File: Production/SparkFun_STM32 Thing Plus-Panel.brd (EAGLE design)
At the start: 145 x 106.7 mm, 998 parts, among them J10 QWIIC_RA, J13 CORTEX_DEBUG, J14 MICRO-SD, J17 QWIIC_RA, J20 CORTEX_DEBUG, J21 MICRO-SD, J24 QWIIC_RA, J27 CORTEX_DEBUG, J28 MICRO-SD, J3 QWIIC_RA, J31 QWIIC_RA, J34 CORTEX_DEBUG, J35 MICRO-SD, J38 QWIIC_RA, J41 CORTEX_DEBUG, J42 MICRO-SD, J45 QWIIC_RA, J48 CORTEX_DEBUG, J49 MICRO-SD, J52 QWIIC_RA, J55 CORTEX_DEBUG, J56 MICRO-SD, J6 CORTEX_DEBUG, J7 MICRO-SD, U1 MCP73831, U10 MCP73831, U11 3.3V, U12 W25QXX128MBIT-6X5, U13 STM32F405RGT6, U14 MCP73831, U15 3.3V, U16 W25QXX128MBIT-6X5, U17 STM32F405RGT6, U18 MCP73831, U19 3.3V, U2 3.3V, U20 W25QXX128MBIT-6X5, U21 STM32F405RGT6, U22 MCP73831, U23 3.3V, U24 W25QXX128MBIT-6X5, U25 STM32F405RGT6, U26 MCP73831, U27 3.3V, U28 W25QXX128MBIT-6X5, U29 STM32F405RGT6, U3 W25QXX128MBIT-6X5, U30 MCP73831, U31 3.3V, U32 W25QXX128MBIT-6X5, U4 STM32F405RGT6, U5 STM32F405RGT6, U6 MCP73831, U7 3.3V, U8 W25QXX128MBIT-6X5, U9 STM32F405RGT6, Y1 32.768kHz, Y10 12MHz, Y11 32.768kHz, Y12 12MHz, Y13 32.768kHz, Y14 12MHz, Y15 32.768kHz, Y16 12MHz, Y2 12MHz, Y3 32.768kHz, Y4 12MHz, Y5 32.768kHz, Y6 12MHz, Y7 32.768kHz, Y8 12MHz, Y9 32.768kHz

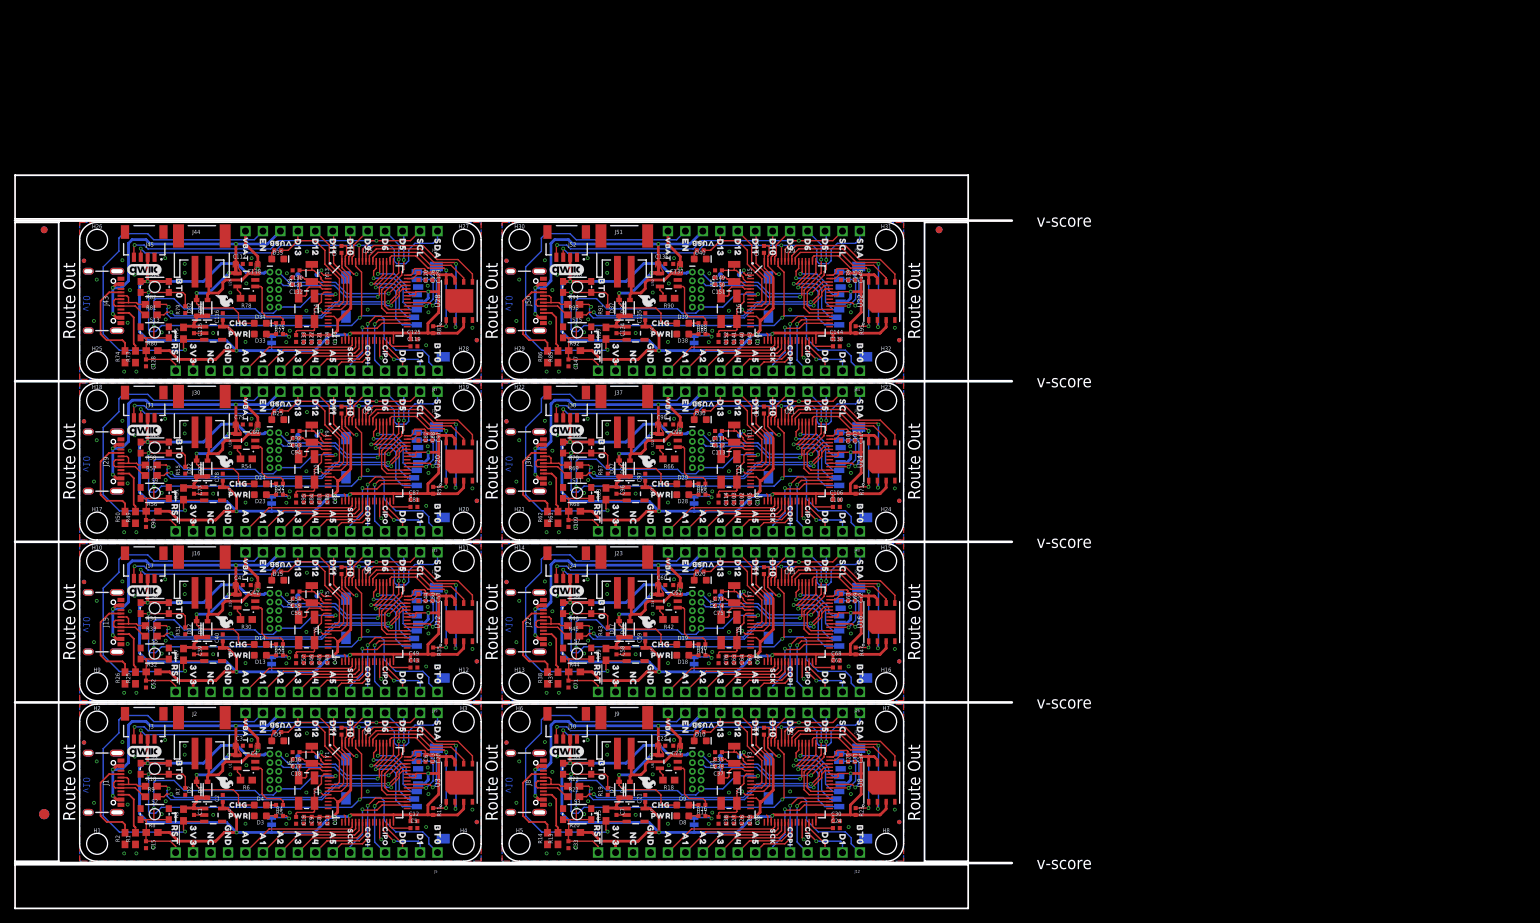
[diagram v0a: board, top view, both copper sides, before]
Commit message: Updated Panel
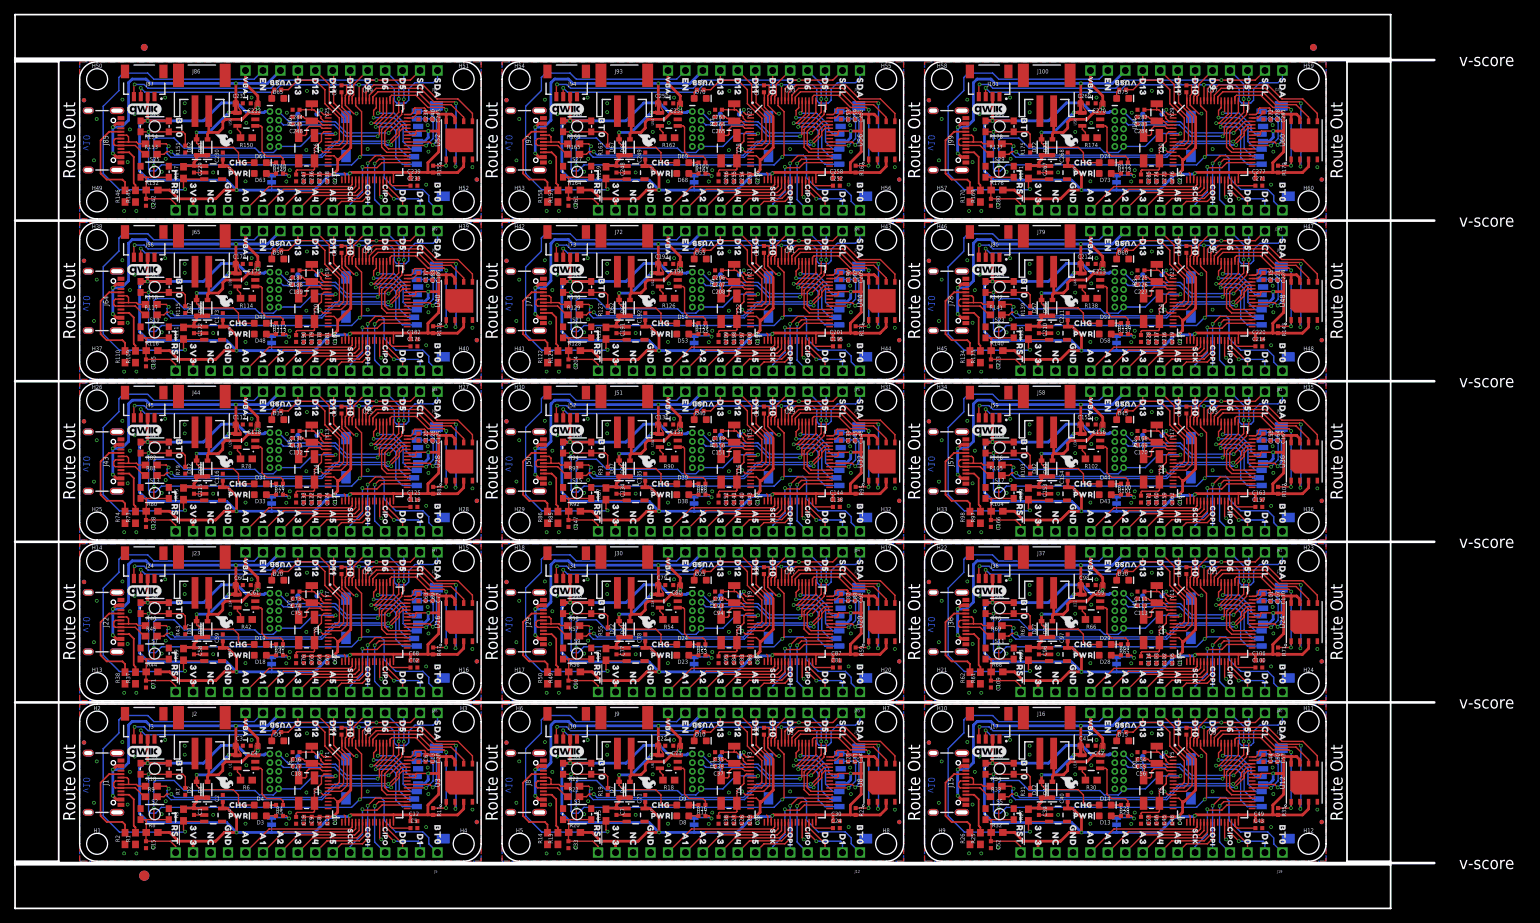
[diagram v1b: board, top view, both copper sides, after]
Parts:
- added C153, C154, C160, C172, C173, C179, C191, C192, C198, C210, C211, C217, C229, C230, C236, C248, C249, C255, C267, C268, C274: 1.0uF, SparkFun-Capacitors:0402-TIGHT
- added C155, C156, C161, C174, C175, C180, C193, C194, C199, C212, C213, C218, C231, C232, C237, C250, C251, C256, C269, C270, C275: 4.7uF, SparkFun-Capacitors:0402-TIGHT
- added C157, C158, C176, C177, C195, C196, C214, C215, C233, C234, C252, C253, C271, C272: 2.2uF, SparkFun-Capacitors:0402-TIGHT
- added C159, C162, C163, C164, C165, C166, C167, C178, C181, C182, C183, C184, C185, C186, C197, C200, C201, C202, C203, C204, C205, C216, C219, C220, C221, C222, C223, C224, C235, C238, C239, C240, C241, C242, C243, C254, C257, C258, C259, C260, C261, C262, C273, C276, C277, C278, C279, C280, C281: 0.1uF, SparkFun-Capacitors:0402-TIGHT
- added C168, C169, C187, C188, C206, C207, C225, C226, C244, C245, C263, C264, C282, C283: 15pF, SparkFun-Capacitors:0402-TIGHT
- added C170, C171, C189, C190, C208, C209, C227, C228, C246, C247, C265, C266, C284, C285: 22pF, SparkFun-Capacitors:0402-TIGHT
- added D41, D42, D46, D47, D51, D52, D56, D57, D61, D62, D66, D67, D71, D72: 3A/10V/280mV, SparkFun-DiscreteSemi:SOD-323
- added D43, D48, D53, D58, D63, D68, D73: RED, SparkFun-LED:LED-0603
- added D44, D49, D54, D59, D64, D69, D74: Yellow, SparkFun-LED:LED-0603
- added D45, D50, D55, D60, D65, D70, D75: BLUE, SparkFun-LED:LED-0603
- added FD33, FD34, FD35, FD36, FD37, FD38, FD39, FD40, FD41, FD42, FD43, FD44, FD45, FD46, FD47, FD48, FD49, FD50, FD51, FD52, FD53, FD54, FD55, FD56, FD57, FD58, FD59, FD60: FIDUCIALUFIDUCIAL, SparkFun-Aesthetics:FIDUCIAL-MICRO
- added H33, H34, H35, H36, H37, H38, H39, H40, H41, H42, H43, H44, H45, H46, H47, H48, H49, H50, H51, H52, H53, H54, H55, H56, H57, H58, H59, H60: STAND-OFFTIGHT, SparkFun-Hardware:STAND-OFF-TIGHT
- added J100, J58, J65, J72, J79, J86, J93: (no value), SparkFun-Connectors:JST-2-SMD
- added J101, J59, J66, J73, J80, J87, J94: QWIIC_RA, SparkFun-Connectors:JST04_1MM_RA
- added J102, J60, J67, J74, J81, J88, J95: (no value), SparkFun-Connectors:1X12_SM_SQ_NOSILK
- added J103, J61, J68, J75, J82, J89, J96: (no value), SparkFun-Connectors:1X16_SM_SQ_NOSILK
- added J104, J62, J69, J76, J83, J90, J97: CORTEX_DEBUG, SparkFun-Connectors:2X5-PTH-1.27MM-NO_SILK
- added J105, J63, J70, J77, J84, J91, J98: MICRO-SD, SparkFun-Connectors:MICRO-SD-SOCKET
- added J57, J64, J71, J78, J85, J92, J99: (no value), SparkFun-Connectors:USB-C-16P-2LAYER-PADS
- added LOGO25, LOGO28, LOGO31, LOGO34, LOGO37, LOGO40, LOGO43: QWIIC_LOGO_5MM, SparkFun-Aesthetics:QWIIC_5MM
- added LOGO26, LOGO29, LOGO32, LOGO35, LOGO38, LOGO41, LOGO44: SFE_LOGO_NAME_FLAME.1_INCH, SparkFun-Aesthetics:SFE_LOGO_NAME_FLAME_.1
- added LOGO27, LOGO30, LOGO33, LOGO36, LOGO39, LOGO42, LOGO45: OSHW-LOGOS, SparkFun-Aesthetics:OSHW-LOGO-S
- added PWR10, PWR11, PWR12, PWR13, PWR14, PWR8, PWR9: (no value), SparkFun-Jumpers:SMT-JUMPER_2_NC_TRACE_NO-SILK
- added R100, R101, R108, R112, R113, R120, R124, R125, R132, R136, R137, R144, R148, R149, R156, R160, R161, R168, R172, R173, R180: 1k, SparkFun-Resistors:0402-TIGHT
- added R102, R114, R126, R138, R150, R162, R174: 2.0k, SparkFun-Resistors:0603
- added R103, R107, R115, R119, R127, R131, R139, R143, R151, R155, R163, R167, R175, R179: 100k, SparkFun-Resistors:0402-TIGHT
- added R104, R116, R128, R140, R152, R164, R176: 4.7k, SparkFun-Resistors:0603
- added R105, R106, R117, R118, R129, R130, R141, R142, R153, R154, R165, R166, R177, R178: 22, SparkFun-Resistors:0603
- added R109, R110, R121, R122, R133, R134, R145, R146, R157, R158, R169, R170, R97, R98: 5.1k, SparkFun-Resistors:0603
- added R111, R123, R135, R147, R159, R171, R99: 10k, SparkFun-Resistors:0603
- added S17, S18, S19, S20, S21, S22, S23, S24, S25, S26, S27, S28, S29, S30: (no value), SparkFun-Switches:TACTILE_SWITCH_SMD_4.6X2.8MM
- added TP17, TP18, TP19, TP20, TP21, TP22, TP23, TP24, TP25, TP26, TP27, TP28, TP29, TP30, VB10, VB11, VB12, VB13, VB14, VB8, VB9: (no value), SparkFun-Connectors:PAD.03X.03
- added U$465, U$523, U$581, U$639, U$697, U$755, U$813: (no value), output:#RST#0
- added U$466, U$524, U$582, U$640, U$698, U$756, U$814: (no value), output:D130
- added U$467, U$507, U$525, U$565, U$583, U$623, U$641, U$681, U$699, U$739, U$757, U$797, U$815, U$855: (no value), output:PWR0
- added U$468, U$526, U$584, U$642, U$700, U$758, U$816: (no value), output:CHG0
- added U$469, U$527, U$585, U$643, U$701, U$759, U$817: (no value), output:##RESET##0
- added U$470, U$528, U$586, U$644, U$702, U$760, U$818: (no value), output:#3V3#0
- added U$471, U$529, U$587, U$645, U$703, U$761, U$819: (no value), output:#NC#0
- added U$472, U$530, U$588, U$646, U$704, U$762, U$820: (no value), output:#GND#0
- added U$473, U$531, U$589, U$647, U$705, U$763, U$821: (no value), output:#A0#0
- added U$474, U$532, U$590, U$648, U$706, U$764, U$822: (no value), output:#A1#0
- added U$475, U$533, U$591, U$649, U$707, U$765, U$823: (no value), output:#A2#0
- added U$476, U$534, U$592, U$650, U$708, U$766, U$824: (no value), output:#A3#0
- added U$477, U$535, U$593, U$651, U$709, U$767, U$825: (no value), output:#A4#0
- added U$478, U$536, U$594, U$652, U$710, U$768, U$826: (no value), output:#A5#0
- added U$479, U$537, U$595, U$653, U$711, U$769, U$827: (no value), output:#D11#0
- added U$480, U$538, U$596, U$654, U$712, U$770, U$828: (no value), output:#D12#0
- added U$481, U$539, U$597, U$655, U$713, U$771, U$829: (no value), output:#D13#0
- added U$482, U$540, U$598, U$656, U$714, U$772, U$830: (no value), output:#VUSB#0
- added U$483, U$541, U$599, U$657, U$715, U$773, U$831: (no value), output:#EN#0
- added U$484, U$542, U$600, U$658, U$716, U$774, U$832: (no value), output:#VBAT#0
- added U$485, U$543, U$601, U$659, U$717, U$775, U$833: (no value), output:3V30
- added U$486, U$544, U$602, U$660, U$718, U$776, U$834: (no value), output:NC0
- added U$487, U$545, U$603, U$661, U$719, U$777, U$835: (no value), output:GND0
- added U$488, U$546, U$604, U$662, U$720, U$778, U$836: (no value), output:A00
- added U$489, U$547, U$605, U$663, U$721, U$779, U$837: (no value), output:A10
- added U$490, U$548, U$606, U$664, U$722, U$780, U$838: (no value), output:A20
- added U$491, U$549, U$607, U$665, U$723, U$781, U$839: (no value), output:A30
- added U$492, U$550, U$608, U$666, U$724, U$782, U$840: (no value), output:A40
- added U$493, U$551, U$609, U$667, U$725, U$783, U$841: (no value), output:A50
- added U$494, U$552, U$610, U$668, U$726, U$784, U$842: (no value), output:D00
- added U$495, U$553, U$611, U$669, U$727, U$785, U$843: (no value), output:D10
- added U$496, U$503, U$554, U$561, U$612, U$619, U$670, U$677, U$728, U$735, U$786, U$793, U$844, U$851: (no value), output:BT00
- added U$497, U$555, U$613, U$671, U$729, U$787, U$845: (no value), output:D50
- added U$498, U$556, U$614, U$672, U$730, U$788, U$846: (no value), output:D60
- added U$499, U$557, U$615, U$673, U$731, U$789, U$847: (no value), output:D90
- added U$500, U$558, U$616, U$674, U$732, U$790, U$848: (no value), output:D100
- added U$501, U$559, U$617, U$675, U$733, U$791, U$849: (no value), output:D110
- added U$502, U$560, U$618, U$676, U$734, U$792, U$850: (no value), output:D120
- added U$504, U$562, U$620, U$678, U$736, U$794, U$852: (no value), output:SCK0
- added U$505, U$563, U$621, U$679, U$737, U$795, U$853: (no value), output:COPI0
- added U$506, U$564, U$622, U$680, U$738, U$796, U$854: (no value), output:CIPO0
- added U$508, U$566, U$624, U$682, U$740, U$798, U$856: (no value), output:SCL_0
- added U$509, U$567, U$625, U$683, U$741, U$799, U$857: (no value), output:SDA_0
- added U$510, U$568, U$626, U$684, U$742, U$800, U$858: (no value), output:VBAT_0
- added U$511, U$569, U$627, U$685, U$743, U$801, U$859: (no value), output:EN_0
- added U$512, U$570, U$628, U$686, U$744, U$802, U$860: (no value), output:VUSB0
- added U$513, U$571, U$629, U$687, U$745, U$803, U$861: (no value), output:STM320
- added U$514, U$572, U$630, U$688, U$746, U$804, U$862: (no value), output:THING_PLUS0
- added U$515, U$573, U$631, U$689, U$747, U$805, U$863: (no value), output:STM32F405RG0
- added U$516, U$574, U$632, U$690, U$748, U$806, U$864: (no value), SparkFun-Aesthetics:SFE_LOGO_FLAME_.1
- added U$517, U$575, U$633, U$691, U$749, U$807, U$865: (no value), buzzard_labels:D53
- added U$518, U$576, U$634, U$692, U$750, U$808, U$866: (no value), buzzard_labels:D62
- added U$519, U$577, U$635, U$693, U$751, U$809, U$867: (no value), buzzard_labels:D91
- added U$520, U$578, U$636, U$694, U$752, U$810, U$868: (no value), buzzard_labels:D100
- added U$521, U$579, U$637, U$695, U$753, U$811, U$869: (no value), buzzard_labels:SCL4
- added U$522, U$580, U$638, U$696, U$754, U$812, U$870: (no value), buzzard_labels:SDA5
- added U33, U37, U41, U45, U49, U53, U57: STM32F405RGT6, STM32_Temp:TQFP64
- added U34, U38, U42, U46, U50, U54, U58: MCP73831, SparkFun-IC-Power:SOT23-5
- added U35, U39, U43, U47, U51, U55, U59: 3.3V, SparkFun-IC-Power:SOT23-5
- added U36, U40, U44, U48, U52, U56, U60: W25QXX128MBIT-6X5, SparkFun-MicroMod:WSON-8-6X5
- added Y17, Y19, Y21, Y23, Y25, Y27, Y29: 32.768kHz, SparkFun-Clocks:CRYSTAL-SMD-3.2X1.5MM
- added Y18, Y20, Y22, Y24, Y26, Y28, Y30: 12MHz, SparkFun-Clocks:CRYSTAL-SMD-5X3.2-4PAD
- moved C39 125.1 mm to (139.6, 7.24)
- moved C40 125.1 mm to (143.8, 9.14)
- moved C42 125.1 mm to (148.3, 16.8)
- moved C43 125.1 mm to (171.6, 4.83)
- moved C44 125.1 mm to (172.2, 15.0)
- moved C49 125.1 mm to (171.6, 5.84)
- moved C50 125.1 mm to (173.3, 15.0)
- moved C51 125.1 mm to (161.0, 18.9)
- moved C53 125.1 mm to (174.2, 15.0)
- moved C54 125.1 mm to (154.4, 15.9)
- moved C55 125.1 mm to (154.4, 14.9)
- moved C56 125.1 mm to (154.4, 13.8)
- moved D11 125.1 mm to (141.5, 10.4)
- moved D12 125.1 mm to (140.0, 10.4)
- moved FD11 125.1 mm to (180.7, 5.71)
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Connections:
- new net !RESET10: C204.1, J75.16, J76.10, R128.1, S21.1, S21.2, U41.7
- new net !RESET11: C223.1, J82.16, J83.10, R140.1, S23.1, S23.2, U45.7
- new net !RESET12: C242.1, J89.16, J90.10, R152.1, S25.1, S25.2, U49.7
- new net !RESET13: C261.1, J96.16, J97.10, R164.1, S27.1, S27.2, U53.7
- new net !RESET14: C280.1, J103.16, J104.10, R176.1, S29.1, S29.2, U57.7
- new net !RESET8: C166.1, J61.16, J62.10, R104.1, S17.1, S17.2, U33.7
- new net !RESET9: C185.1, J68.16, J69.10, R116.1, S19.1, S19.2, U37.7
- new net 3.3V10: C192.1, C197.1, C198.1, C199.1, C200.1, C201.1, C202.1, C203.1, C205.1, J73.2, J75.15, J76.1, J77.VCC, PWR10.2, R128.2, R131.2, S22.3, S22.4, U41.13, U41.19, U41.32, U41.42, U41.43, U41.48, U41.64, U43.5, U44.3, U44.7, U44.8
- new net 3.3V11: C211.1, C216.1, C217.1, C218.1, C219.1, C220.1, C221.1, C222.1, C224.1, J80.2, J82.15, J83.1, J84.VCC, PWR11.2, R140.2, R143.2, S24.3, S24.4, U45.13, U45.19, U45.32, U45.42, U45.43, U45.48, U45.64, U47.5, U48.3, U48.7, U48.8
- new net 3.3V12: C230.1, C235.1, C236.1, C237.1, C238.1, C239.1, C240.1, C241.1, C243.1, J87.2, J89.15, J90.1, J91.VCC, PWR12.2, R152.2, R155.2, S26.3, S26.4, U49.13, U49.19, U49.32, U49.42, U49.43, U49.48, U49.64, U51.5, U52.3, U52.7, U52.8
- new net 3.3V13: C249.1, C254.1, C255.1, C256.1, C257.1, C258.1, C259.1, C260.1, C262.1, J94.2, J96.15, J97.1, J98.VCC, PWR13.2, R164.2, R167.2, S28.3, S28.4, U53.13, U53.19, U53.32, U53.42, U53.43, U53.48, U53.64, U55.5, U56.3, U56.7, U56.8
- new net 3.3V14: C268.1, C273.1, C274.1, C275.1, C276.1, C277.1, C278.1, C279.1, C281.1, J101.2, J103.15, J104.1, J105.VCC, PWR14.2, R176.2, R179.2, S30.3, S30.4, U57.13, U57.19, U57.32, U57.42, U57.43, U57.48, U57.64, U59.5, U60.3, U60.7, U60.8
- new net 3.3V8: C154.1, C159.1, C160.1, C161.1, C162.1, C163.1, C164.1, C165.1, C167.1, J59.2, J61.15, J62.1, J63.VCC, PWR8.2, R104.2, R107.2, S18.3, S18.4, U33.13, U33.19, U33.32, U33.42, U33.43, U33.48, U33.64, U35.5, U36.3, U36.7, U36.8
- new net 3.3V9: C173.1, C178.1, C179.1, C180.1, C181.1, C182.1, C183.1, C184.1, C186.1, J66.2, J68.15, J69.1, J70.VCC, PWR9.2, R116.2, R119.2, S20.3, S20.4, U37.13, U37.19, U37.32, U37.42, U37.43, U37.48, U37.64, U39.5, U40.3, U40.7, U40.8
- new net 32KHZ_IN10: C206.1, U41.3, Y21.P$1
- new net 32KHZ_IN11: C225.1, U45.3, Y23.P$1
- new net 32KHZ_IN12: C244.1, U49.3, Y25.P$1
- new net 32KHZ_IN13: C263.1, U53.3, Y27.P$1
- new net 32KHZ_IN14: C282.1, U57.3, Y29.P$1
- new net 32KHZ_IN8: C168.1, U33.3, Y17.P$1
- new net 32KHZ_IN9: C187.1, U37.3, Y19.P$1
- new net 32KHZ_OUT10: C207.1, U41.4, Y21.P$2
- new net 32KHZ_OUT11: C226.1, U45.4, Y23.P$2
- new net 32KHZ_OUT12: C245.1, U49.4, Y25.P$2
- new net 32KHZ_OUT13: C264.1, U53.4, Y27.P$2
- new net 32KHZ_OUT14: C283.1, U57.4, Y29.P$2
- new net 32KHZ_OUT8: C169.1, U33.4, Y17.P$2
- new net 32KHZ_OUT9: C188.1, U37.4, Y19.P$2
- new net A48: J61.12, U33.20
- new net A49: J61.11, U33.21
- new net A50: J61.10, U33.22
- new net A51: J61.9, U33.23
- new net A52: J61.8, U33.24
- new net A53: J61.7, U33.25
- new net A54: J68.12, U37.20
- new net A55: J68.11, U37.21
- new net A56: J68.10, U37.22
- new net A57: J68.9, U37.23
- new net A58: J68.8, U37.24
- new net A59: J68.7, U37.25
- new net A60: J75.12, U41.20
- new net A61: J75.11, U41.21
- new net A62: J75.10, U41.22
- new net A63: J75.9, U41.23
- new net A64: J75.8, U41.24
- new net A65: J75.7, U41.25
- new net A66: J82.12, U45.20
- new net A67: J82.11, U45.21
- new net A68: J82.10, U45.22
- new net A69: J82.9, U45.23
- new net A70: J82.8, U45.24
- new net A71: J82.7, U45.25
- new net A72: J89.12, U49.20
- new net A73: J89.11, U49.21
- new net A74: J89.10, U49.22
- new net A75: J89.9, U49.23
- new net A76: J89.8, U49.24
- new net A77: J89.7, U49.25
- new net A78: J96.12, U53.20
- new net A79: J96.11, U53.21
- new net A80: J96.10, U53.22
- new net A81: J96.9, U53.23
- new net A82: J96.8, U53.24
- new net A83: J96.7, U53.25
- new net A84: J103.12, U57.20
- new net A85: J103.11, U57.21
- new net A86: J103.10, U57.22
- new net A87: J103.9, U57.23
- new net A88: J103.8, U57.24
- new net A89: J103.7, U57.25
- new net BOOT10: J75.1, R127.2, S22.1, S22.2, U41.60
- new net BOOT11: J82.1, R139.2, S24.1, S24.2, U45.60
- new net BOOT12: J89.1, R151.2, S26.1, S26.2, U49.60
- new net BOOT13: J96.1, R163.2, S28.1, S28.2, U53.60
- new net BOOT14: J103.1, R175.2, S30.1, S30.2, U57.60
- new net BOOT8: J61.1, R103.2, S18.1, S18.2, U33.60
- new net BOOT9: J68.1, R115.2, S20.1, S20.2, U37.60
- new net CIPO10: J75.4, U41.35
- new net CIPO11: J82.4, U45.35
- new net CIPO12: J89.4, U49.35
- new net CIPO13: J96.4, U53.35
- new net CIPO14: J103.4, U57.35
- new net CIPO8: J61.4, U33.35
- new net CIPO9: J68.4, U37.35
- new net COPI10: J75.5, U41.36
- new net COPI11: J82.5, U45.36
- new net COPI12: J89.5, U49.36
- new net COPI13: J96.5, U53.36
- new net COPI14: J103.5, U57.36
- new net COPI8: J61.5, U33.36
- new net COPI9: J68.5, U37.36
- new net D+10: R129.2, U41.45
- new net D+11: R141.2, U45.45
- new net D+12: R153.2, U49.45
- new net D+13: R165.2, U53.45
- new net D+14: R177.2, U57.45
- new net D+8: R105.2, U33.45
- new net D+9: R117.2, U37.45
- new net D-10: R130.2, U41.44
- new net D-11: R142.2, U45.44
- new net D-12: R154.2, U49.44
- new net D-13: R166.2, U53.44
- new net D-14: R178.2, U57.44
- new net D-8: R106.2, U33.44
- new net D-9: R118.2, U37.44
- new net D0/RX10: J75.3, U41.30
- new net D0/RX11: J82.3, U45.30
- new net D0/RX12: J89.3, U49.30
- new net D0/RX13: J96.3, U53.30
- new net D0/RX14: J103.3, U57.30
- new net D0/RX8: J61.3, U33.30
- new net D0/RX9: J68.3, U37.30
- new net D1/TX10: J75.2, U41.29
- new net D1/TX11: J82.2, U45.29
- new net D1/TX12: J89.2, U49.29
- new net D1/TX13: J96.2, U53.29
- new net D1/TX14: J103.2, U57.29
- new net D1/TX8: J61.2, U33.29
- new net D1/TX9: J68.2, U37.29
- new net D100: J102.8, U57.10
- new net D101: J102.7, U57.11
- new net D102: J102.6, U57.62
- new net D103: J102.5, U57.61
- new net D104: J102.4, U57.37
- new net D105: J102.3, U57.38
- new net D57: J60.9, R108.2, U33.9
- new net D58: J60.8, U33.10
- new net D59: J60.7, U33.11
- new net D60: J60.6, U33.62
- new net D61: J60.5, U33.61
- new net D62: J60.4, U33.37
- new net D63: J60.3, U33.38
- new net D64: J67.9, R120.2, U37.9
- new net D65: J67.8, U37.10
- new net D66: J67.7, U37.11
- new net D67: J67.6, U37.62
- new net D68: J67.5, U37.61
- new net D69: J67.4, U37.37
- new net D70: J67.3, U37.38
- new net D71: J74.9, R132.2, U41.9
- new net D72: J74.8, U41.10
- new net D73: J74.7, U41.11
- new net D74: J74.6, U41.62
- new net D75: J74.5, U41.61
- new net D76: J74.4, U41.37
- new net D77: J74.3, U41.38
- new net D78: J81.9, R144.2, U45.9
- new net D79: J81.8, U45.10
- new net D80: J81.7, U45.11
- new net D81: J81.6, U45.62
- new net D82: J81.5, U45.61
- new net D83: J81.4, U45.37
- new net D84: J81.3, U45.38
- new net D85: J88.9, R156.2, U49.9
- new net D86: J88.8, U49.10
- new net D87: J88.7, U49.11
- new net D88: J88.6, U49.62
- new net D89: J88.5, U49.61
- new net D90: J88.4, U49.37
- new net D91: J88.3, U49.38
- new net D92: J95.9, R168.2, U53.9
- new net D93: J95.8, U53.10
- new net D94: J95.7, U53.11
- new net D95: J95.6, U53.62
- new net D96: J95.5, U53.61
- new net D97: J95.4, U53.37
- new net D98: J95.3, U53.38
- new net D99: J102.9, R180.2, U57.9
- new net EN10: J74.11, R123.1, U43.3
- new net EN11: J81.11, R135.1, U47.3
- new net EN12: J88.11, R147.1, U51.3
- new net EN13: J95.11, R159.1, U55.3
- new net EN14: J102.11, R171.1, U59.3
- new net EN8: J60.11, R99.1, U35.3
- new net EN9: J67.11, R111.1, U39.3
- new net FLASH_!CS10: R131.1, U41.50, U44.1
- new net FLASH_!CS11: R143.1, U45.50, U48.1
- new net FLASH_!CS12: R155.1, U49.50, U52.1
- new net FLASH_!CS13: R167.1, U53.50, U56.1
- new net FLASH_!CS14: R179.1, U57.50, U60.1
- new net FLASH_!CS8: R107.1, U33.50, U36.1
- new net FLASH_!CS9: R119.1, U37.50, U40.1
- new net FLASH_SCK10: U41.55, U44.6
- new net FLASH_SCK11: U45.55, U48.6
- new net FLASH_SCK12: U49.55, U52.6
- new net FLASH_SCK13: U53.55, U56.6
- new net FLASH_SCK14: U57.55, U60.6
- new net FLASH_SCK8: U33.55, U36.6
- new net FLASH_SCK9: U37.55, U40.6
- new net FLASH_SDI10: U41.57, U44.5
- new net FLASH_SDI11: U45.57, U48.5
- new net FLASH_SDI12: U49.57, U52.5
- new net FLASH_SDI13: U53.57, U56.5
- new net FLASH_SDI14: U57.57, U60.5
- new net FLASH_SDI8: U33.57, U36.5
- new net FLASH_SDI9: U37.57, U40.5
- new net FLASH_SDO10: U41.56, U44.2
- new net FLASH_SDO11: U45.56, U48.2
- new net FLASH_SDO12: U49.56, U52.2
- new net FLASH_SDO13: U53.56, U56.2
- new net FLASH_SDO14: U57.56, U60.2
- new net FLASH_SDO8: U33.56, U36.2
- new net FLASH_SDO9: U37.56, U40.2
- new net GND10: C191.2, C192.2, C193.2, C194.2, C195.2, C196.2, C197.2, C198.2, C199.2, C200.2, C201.2, C202.2, C203.2, C204.2, C205.2, C206.2, C207.2, C208.2, C209.2, D53.C, D55.C, J71.GND, J71.GND2, J71.SHLD1, J71.SHLD2, J71.SHLD3, J71.SHLD4, J72.1, J73.1, J75.13, J76.3, J76.5, J76.9, J77.CD1, J77.GND, J77.GND1, J77.GND3, R121.1, R122.1, R126.1, R127.1, S21.3, S21.4, U41.12, U41.18, U41.28, U41.63, U42.2, U43.2, U44.4
- new net GND11: C210.2, C211.2, C212.2, C213.2, C214.2, C215.2, C216.2, C217.2, C218.2, C219.2, C220.2, C221.2, C222.2, C223.2, C224.2, C225.2, C226.2, C227.2, C228.2, D58.C, D60.C, J78.GND, J78.GND2, J78.SHLD1, J78.SHLD2, J78.SHLD3, J78.SHLD4, J79.1, J80.1, J82.13, J83.3, J83.5, J83.9, J84.CD1, J84.GND, J84.GND1, J84.GND3, R133.1, R134.1, R138.1, R139.1, S23.3, S23.4, U45.12, U45.18, U45.28, U45.63, U46.2, U47.2, U48.4
- new net GND12: C229.2, C230.2, C231.2, C232.2, C233.2, C234.2, C235.2, C236.2, C237.2, C238.2, C239.2, C240.2, C241.2, C242.2, C243.2, C244.2, C245.2, C246.2, C247.2, D63.C, D65.C, J85.GND, J85.GND2, J85.SHLD1, J85.SHLD2, J85.SHLD3, J85.SHLD4, J86.1, J87.1, J89.13, J90.3, J90.5, J90.9, J91.CD1, J91.GND, J91.GND1, J91.GND3, R145.1, R146.1, R150.1, R151.1, S25.3, S25.4, U49.12, U49.18, U49.28, U49.63, U50.2, U51.2, U52.4
- new net GND13: C248.2, C249.2, C250.2, C251.2, C252.2, C253.2, C254.2, C255.2, C256.2, C257.2, C258.2, C259.2, C260.2, C261.2, C262.2, C263.2, C264.2, C265.2, C266.2, D68.C, D70.C, J92.GND, J92.GND2, J92.SHLD1, J92.SHLD2, J92.SHLD3, J92.SHLD4, J93.1, J94.1, J96.13, J97.3, J97.5, J97.9, J98.CD1, J98.GND, J98.GND1, J98.GND3, R157.1, R158.1, R162.1, R163.1, S27.3, S27.4, U53.12, U53.18, U53.28, U53.63, U54.2, U55.2, U56.4
- new net GND14: C267.2, C268.2, C269.2, C270.2, C271.2, C272.2, C273.2, C274.2, C275.2, C276.2, C277.2, C278.2, C279.2, C280.2, C281.2, C282.2, C283.2, C284.2, C285.2, D73.C, D75.C, J100.1, J101.1, J103.13, J104.3, J104.5, J104.9, J105.CD1, J105.GND, J105.GND1, J105.GND3, J99.GND, J99.GND2, J99.SHLD1, J99.SHLD2, J99.SHLD3, J99.SHLD4, R169.1, R170.1, R174.1, R175.1, S29.3, S29.4, U57.12, U57.18, U57.28, U57.63, U58.2, U59.2, U60.4
- new net GND8: C153.2, C154.2, C155.2, C156.2, C157.2, C158.2, C159.2, C160.2, C161.2, C162.2, C163.2, C164.2, C165.2, C166.2, C167.2, C168.2, C169.2, C170.2, C171.2, D43.C, D45.C, J57.GND, J57.GND2, J57.SHLD1, J57.SHLD2, J57.SHLD3, J57.SHLD4, J58.1, J59.1, J61.13, J62.3, J62.5, J62.9, J63.CD1, J63.GND, J63.GND1, J63.GND3, R102.1, R103.1, R97.1, R98.1, S17.3, S17.4, U33.12, U33.18, U33.28, U33.63, U34.2, U35.2, U36.4
- new net GND9: C172.2, C173.2, C174.2, C175.2, C176.2, C177.2, C178.2, C179.2, C180.2, C181.2, C182.2, C183.2, C184.2, C185.2, C186.2, C187.2, C188.2, C189.2, C190.2, D48.C, D50.C, J64.GND, J64.GND2, J64.SHLD1, J64.SHLD2, J64.SHLD3, J64.SHLD4, J65.1, J66.1, J68.13, J69.3, J69.5, J69.9, J70.CD1, J70.GND, J70.GND1, J70.GND3, R109.1, R110.1, R114.1, R115.1, S19.3, S19.4, U37.12, U37.18, U37.28, U37.63, U38.2, U39.2, U40.4
- new net N$100: R102.2, U34.5
- new net N$101: D44.C, R101.2
- new net N$102: R101.1, U34.1
- new net N$103: C157.1, U33.31
- new net N$104: C158.1, U33.47
- new net N$105: J57.A6, J57.B6, R105.1
- new net N$106: J57.A7, J57.B7, R106.1
- new net N$107: D45.A, R108.1
- new net N$108: PWR8.1, R100.2
- new net N$109: J64.A5, R110.2
- new net N$110: J64.B5, R109.2
- new net N$111: D48.A, R112.1
- new net N$112: R114.2, U38.5
- new net N$113: D49.C, R113.2
- new net N$114: R113.1, U38.1
- new net N$115: C176.1, U37.31
- new net N$116: C177.1, U37.47
- new net N$117: J64.A6, J64.B6, R117.1
- new net N$118: J64.A7, J64.B7, R118.1
- new net N$119: D50.A, R120.1
- new net N$120: PWR9.1, R112.2
- new net N$121: J71.A5, R122.2
- new net N$122: J71.B5, R121.2
- new net N$123: D53.A, R124.1
- new net N$124: R126.2, U42.5
- new net N$125: D54.C, R125.2
- new net N$126: R125.1, U42.1
- new net N$127: C195.1, U41.31
- new net N$128: C196.1, U41.47
- new net N$129: J71.A6, J71.B6, R129.1
- new net N$130: J71.A7, J71.B7, R130.1
- new net N$131: D55.A, R132.1
- new net N$132: PWR10.1, R124.2
- new net N$133: J78.A5, R134.2
- new net N$134: J78.B5, R133.2
- new net N$135: D58.A, R136.1
- new net N$136: R138.2, U46.5
- new net N$137: D59.C, R137.2
- new net N$138: R137.1, U46.1
- new net N$139: C214.1, U45.31
- new net N$140: C215.1, U45.47
- new net N$141: J78.A6, J78.B6, R141.1
- new net N$142: J78.A7, J78.B7, R142.1
- new net N$143: D60.A, R144.1
- new net N$144: PWR11.1, R136.2
- new net N$145: J85.A5, R146.2
- new net N$146: J85.B5, R145.2
- new net N$147: D63.A, R148.1
- new net N$148: R150.2, U50.5
- new net N$149: D64.C, R149.2
- new net N$150: R149.1, U50.1
- new net N$151: C233.1, U49.31
- new net N$152: C234.1, U49.47
- new net N$153: J85.A6, J85.B6, R153.1
- new net N$154: J85.A7, J85.B7, R154.1
- new net N$155: D65.A, R156.1
- new net N$156: PWR12.1, R148.2
- new net N$157: J92.A5, R158.2
- new net N$158: J92.B5, R157.2
- new net N$159: D68.A, R160.1
- new net N$160: R162.2, U54.5
- new net N$161: D69.C, R161.2
- new net N$162: R161.1, U54.1
- new net N$163: C252.1, U53.31
- new net N$164: C253.1, U53.47
- new net N$165: J92.A6, J92.B6, R165.1
- new net N$166: J92.A7, J92.B7, R166.1
- new net N$167: D70.A, R168.1
- new net N$168: PWR13.1, R160.2
- new net N$169: J99.A5, R170.2
- new net N$170: J99.B5, R169.2
- new net N$171: D73.A, R172.1
- new net N$172: R174.2, U58.5
- new net N$173: D74.C, R173.2
- new net N$174: R173.1, U58.1
- new net N$175: C271.1, U57.31
- new net N$176: C272.1, U57.47
- new net N$177: J99.A6, J99.B6, R177.1
- new net N$178: J99.A7, J99.B7, R178.1
- new net N$179: D75.A, R180.1
- new net N$180: PWR14.1, R172.2
- new net N$97: J57.A5, R98.2
- new net N$98: J57.B5, R97.2
- new net N$99: D43.A, R100.1
- new net OSC_IN10: C208.1, U41.5, Y22.1
- new net OSC_IN11: C227.1, U45.5, Y24.1
- new net OSC_IN12: C246.1, U49.5, Y26.1
- new net OSC_IN13: C265.1, U53.5, Y28.1
- new net OSC_IN14: C284.1, U57.5, Y30.1
- new net OSC_IN8: C170.1, U33.5, Y18.1
- new net OSC_IN9: C189.1, U37.5, Y20.1
- new net OSC_OUT10: C209.1, U41.6, Y22.3
- new net OSC_OUT11: C228.1, U45.6, Y24.3
- new net OSC_OUT12: C247.1, U49.6, Y26.3
- new net OSC_OUT13: C266.1, U53.6, Y28.3
- new net OSC_OUT14: C285.1, U57.6, Y30.3
- new net OSC_OUT8: C171.1, U33.6, Y18.3
- new net OSC_OUT9: C190.1, U37.6, Y20.3
- new net SCK10: J75.6, U41.34
- new net SCK11: J82.6, U45.34
- new net SCK12: J89.6, U49.34
- new net SCK13: J96.6, U53.34
- new net SCK14: J103.6, U57.34
- new net SCK8: J61.6, U33.34
- new net SCK9: J68.6, U37.34
- new net SCL10: J73.4, J74.2, U41.58
- new net SCL11: J80.4, J81.2, U45.58
- new net SCL12: J87.4, J88.2, U49.58
- new net SCL13: J94.4, J95.2, U53.58
- new net SCL14: J101.4, J102.2, U57.58
- new net SCL8: J59.4, J60.2, U33.58
- new net SCL9: J66.4, J67.2, U37.58
- new net SDA10: J73.3, J74.1, U41.59
- new net SDA11: J80.3, J81.1, U45.59
- new net SDA12: J87.3, J88.1, U49.59
- new net SDA13: J94.3, J95.1, U53.59
- new net SDA14: J101.3, J102.1, U57.59
- new net SDA8: J59.3, J60.1, U33.59
- new net SDA9: J66.3, J67.1, U37.59
- new net SDIO_CLK10: J77.SCLK, U41.53
- new net SDIO_CLK11: J84.SCLK, U45.53
- new net SDIO_CLK12: J91.SCLK, U49.53
- new net SDIO_CLK13: J98.SCLK, U53.53
- new net SDIO_CLK14: J105.SCLK, U57.53
- new net SDIO_CLK8: J63.SCLK, U33.53
- new net SDIO_CLK9: J70.SCLK, U37.53
- new net SDIO_CMD10: J77.DI/CMD, U41.54
- new net SDIO_CMD11: J84.DI/CMD, U45.54
- new net SDIO_CMD12: J91.DI/CMD, U49.54
- new net SDIO_CMD13: J98.DI/CMD, U53.54
- new net SDIO_CMD14: J105.DI/CMD, U57.54
- new net SDIO_CMD8: J63.DI/CMD, U33.54
- new net SDIO_CMD9: J70.DI/CMD, U37.54
- new net SDIO_D32: J63.CS/DAT3, U33.52
- new net SDIO_D33: J63.DAT2, U33.51
- new net SDIO_D34: J63.DAT1, U33.40
- new net SDIO_D35: J63.DO/DAT0, U33.39
- new net SDIO_D36: J70.CS/DAT3, U37.52
- new net SDIO_D37: J70.DAT2, U37.51
- new net SDIO_D38: J70.DAT1, U37.40
- new net SDIO_D39: J70.DO/DAT0, U37.39
- new net SDIO_D40: J77.CS/DAT3, U41.52
- new net SDIO_D41: J77.DAT2, U41.51
- new net SDIO_D42: J77.DAT1, U41.40
- new net SDIO_D43: J77.DO/DAT0, U41.39
- new net SDIO_D44: J84.CS/DAT3, U45.52
- new net SDIO_D45: J84.DAT2, U45.51
- new net SDIO_D46: J84.DAT1, U45.40
- new net SDIO_D47: J84.DO/DAT0, U45.39
- new net SDIO_D48: J91.CS/DAT3, U49.52
- new net SDIO_D49: J91.DAT2, U49.51
- new net SDIO_D50: J91.DAT1, U49.40
- new net SDIO_D51: J91.DO/DAT0, U49.39
- new net SDIO_D52: J98.CS/DAT3, U53.52
- new net SDIO_D53: J98.DAT2, U53.51
- new net SDIO_D54: J98.DAT1, U53.40
- new net SDIO_D55: J98.DO/DAT0, U53.39
- new net SDIO_D56: J105.CS/DAT3, U57.52
- new net SDIO_D57: J105.DAT2, U57.51
- new net SDIO_D58: J105.DAT1, U57.40
- new net SDIO_D59: J105.DO/DAT0, U57.39
- new net SWCLK10: J76.4, TP22.P$1, U41.49
- new net SWCLK11: J83.4, TP24.P$1, U45.49
- new net SWCLK12: J90.4, TP26.P$1, U49.49
- new net SWCLK13: J97.4, TP28.P$1, U53.49
- new net SWCLK14: J104.4, TP30.P$1, U57.49
- new net SWCLK8: J62.4, TP18.P$1, U33.49
- new net SWCLK9: J69.4, TP20.P$1, U37.49
- new net SWDIO10: J76.2, TP21.P$1, U41.46
- new net SWDIO11: J83.2, TP23.P$1, U45.46
- new net SWDIO12: J90.2, TP25.P$1, U49.46
- new net SWDIO13: J97.2, TP27.P$1, U53.46
- new net SWDIO14: J104.2, TP29.P$1, U57.46
- new net SWDIO8: J62.2, TP17.P$1, U33.46
- new net SWDIO9: J69.2, TP19.P$1, U37.46
- new net VB10: U41.1, VB10.P$1
- new net VB11: U45.1, VB11.P$1
- new net VB12: U49.1, VB12.P$1
- new net VB13: U53.1, VB13.P$1
- new net VB14: U57.1, VB14.P$1
- new net VB8: U33.1, VB8.P$1
- new net VB9: U37.1, VB9.P$1
- new net VIN10: C191.1, D51.C, D52.C, R123.2, U43.1
- new net VIN11: C210.1, D56.C, D57.C, R135.2, U47.1
- new net VIN12: C229.1, D61.C, D62.C, R147.2, U51.1
- new net VIN13: C248.1, D66.C, D67.C, R159.2, U55.1
- new net VIN14: C267.1, D71.C, D72.C, R171.2, U59.1
- new net VIN8: C153.1, D41.C, D42.C, R99.2, U35.1
- new net VIN9: C172.1, D46.C, D47.C, R111.2, U39.1
- new net V_BATT10: C194.1, D51.A, J72.2, J74.12, U42.3
- new net V_BATT11: C213.1, D56.A, J79.2, J81.12, U46.3
- new net V_BATT12: C232.1, D61.A, J86.2, J88.12, U50.3
- new net V_BATT13: C251.1, D66.A, J93.2, J95.12, U54.3
- new net V_BATT14: C270.1, D71.A, J100.2, J102.12, U58.3
- new net V_BATT8: C156.1, D41.A, J58.2, J60.12, U34.3
- new net V_BATT9: C175.1, D46.A, J65.2, J67.12, U38.3
- new net V_USB10: C193.1, D52.A, D54.A, J71.VBUS1, J71.VBUS2, J74.10, U42.4
- new net V_USB11: C212.1, D57.A, D59.A, J78.VBUS1, J78.VBUS2, J81.10, U46.4
- new net V_USB12: C231.1, D62.A, D64.A, J85.VBUS1, J85.VBUS2, J88.10, U50.4
- new net V_USB13: C250.1, D67.A, D69.A, J92.VBUS1, J92.VBUS2, J95.10, U54.4
- new net V_USB14: C269.1, D72.A, D74.A, J102.10, J99.VBUS1, J99.VBUS2, U58.4
- new net V_USB8: C155.1, D42.A, D44.A, J57.VBUS1, J57.VBUS2, J60.10, U34.4
- new net V_USB9: C174.1, D47.A, D49.A, J64.VBUS1, J64.VBUS2, J67.10, U38.4
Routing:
- net 3.3V10: track 0.00 -> 157.8 mm, vias 0 -> 5
- net 3.3V9: track 0.00 -> 157.8 mm, vias 0 -> 5
- net 3.3V8: track 0.00 -> 157.8 mm, vias 0 -> 5
- net 3.3V14: track 0.00 -> 157.8 mm, vias 0 -> 5
- net 3.3V13: track 0.00 -> 157.8 mm, vias 0 -> 5
- net 3.3V11: track 0.00 -> 157.8 mm, vias 0 -> 5
- net 3.3V12: track 0.00 -> 157.8 mm, vias 0 -> 5
- net BOOT9: track 0.00 -> 70.9 mm, vias 0 -> 2
- net BOOT11: track 0.00 -> 70.9 mm, vias 0 -> 2
- net BOOT8: track 0.00 -> 70.9 mm, vias 0 -> 2
- net BOOT14: track 0.00 -> 70.9 mm, vias 0 -> 2
- net BOOT13: track 0.00 -> 70.9 mm, vias 0 -> 2
- net BOOT12: track 0.00 -> 70.9 mm, vias 0 -> 2
- net BOOT10: track 0.00 -> 70.9 mm, vias 0 -> 2
- net V_USB14: track 0.00 -> 63.4 mm, vias 0 -> 5
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- added copper zone on layer 1, net GND10
- added copper zone on layer 16, net GND10
- added copper zone on layer 1, net GND11
- added copper zone on layer 16, net GND11
- added copper zone on layer 1, net GND12
- added copper zone on layer 16, net GND12
- added copper zone on layer 1, net GND13
- added copper zone on layer 16, net GND13
- added copper zone on layer 1, net GND14
- added copper zone on layer 16, net GND14
- added copper zone on layer 1, net GND8
- added copper zone on layer 16, net GND8
- added copper zone on layer 1, net GND9
- added copper zone on layer 16, net GND9
- added copper zone on layer 1, net V_BATT10
- added copper zone on layer 1, net V_BATT11
- added copper zone on layer 1, net V_BATT12
- added copper zone on layer 1, net V_BATT13
- added copper zone on layer 1, net V_BATT14
- added copper zone on layer 1, net V_BATT8
- added copper zone on layer 1, net V_BATT9
- added copper zone on layer 1, net V_USB10
- added copper zone on layer 1, net V_USB11
- added copper zone on layer 1, net V_USB12
- added copper zone on layer 1, net V_USB13
- added copper zone on layer 1, net V_USB14
- added copper zone on layer 1, net V_USB8
- added copper zone on layer 1, net V_USB9
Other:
- board size 145 x 106.7 mm -> 206.5 x 130 mm
